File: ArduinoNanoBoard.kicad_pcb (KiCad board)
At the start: 2 copper layers, 121.9 x 81.3 mm, 12 parts, among them J1 Conn_01x15_Male, J2 Conn_01x04_Male, J3 Conn_01x10_Male, J4 Conn_01x08_Male, J5 Conn_01x04_Male

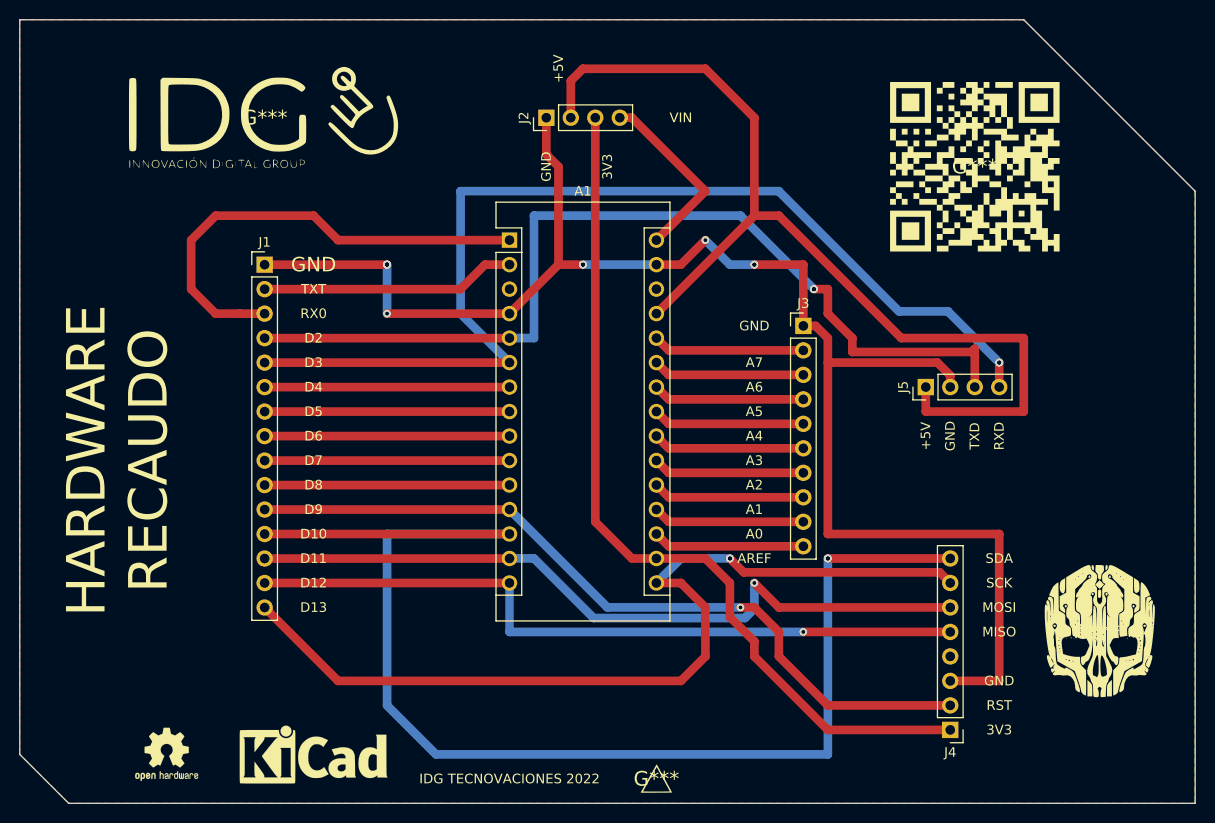
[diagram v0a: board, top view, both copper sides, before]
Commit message: BOPIR05 - ADD HOLES TO PCB
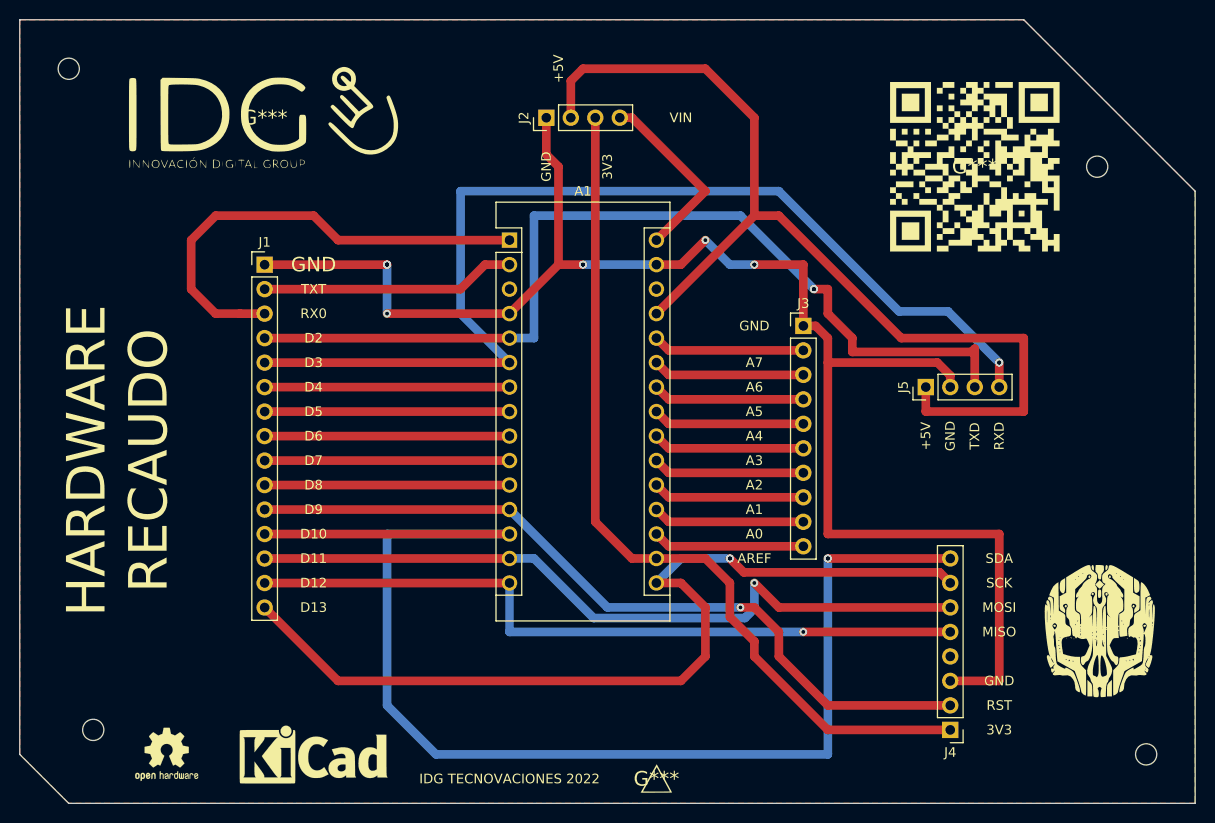
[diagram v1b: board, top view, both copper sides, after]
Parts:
- added REF**: MountingHole_2.2mm_M2, MountingHole:MountingHole_2.2mm_M2, F.Cu at (198.1, 132.1)
- added REF**: MountingHole_2.2mm_M2, MountingHole:MountingHole_2.2mm_M2, F.Cu at (88.9, 129.5)
- added REF**: MountingHole_2.2mm_M2, MountingHole:MountingHole_2.2mm_M2, F.Cu at (86.4, 61.0)
- added REF**: MountingHole_2.2mm_M2, MountingHole:MountingHole_2.2mm_M2, F.Cu at (193.0, 71.1)
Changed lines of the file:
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@@
       (svguseinch false)
       (svgprecision 6)
-      (excludeedgelayer true)
+      (excludeedgelayer false)
       (plotframeref false)
       (viasonmask false)
@@
       (drillshape 0)
       (scaleselection 1)
-      (outputdirectory "")
+      (outputdirectory "../gerberIdg/")
     )
   )
@@
       ) (layer "F.SilkS") (width 0.01) (fill solid))
   )
+  (footprint "MountingHole:MountingHole_2.2mm_M2" (layer "F.Cu")
+    (at 198.12 132.08)
+    (descr "Mounting Hole 2.2mm, no annular, M2")
+    (tags "mounting hole 2.2mm no annular m2")
+    (attr exclude_from_pos_files exclude_from_bom)
+    (fp_text reference "REF**" (at 0 -3.2) (layer "F.SilkS") hide
+      (effects (font (size 1 1) (thickness 0.15)))
+    )
+    (fp_text value "MountingHole_2.2mm_M2" (at 0 3.2) (layer "F.Fab")
+      (effects (font (size 1 1) (thickness 0.15)))
+    )
+    (fp_text user "${REFERENCE}" (at 0.3 0) (layer "F.Fab") hide
+      (effects (font (size 1 1) (thickness 0.15)))
+    )
+    (fp_circle (center 0 0) (end 2.2 0) (layer "Cmts.User") (width 0.15) (fill none))
+    (fp_circle (center 0 0) (end 2.45 0) (layer "F.CrtYd") (width 0.05) (fill none))
+    (pad "" np_thru_hole circle locked (at 0 0) (size 2.2 2.2) (drill 2.2) (layers *.Cu *.Mask))
+  )
   (footprint "Connector_PinHeader_2.54mm:PinHeader_1x08_P2.54mm_Vertical" (layer "F.Cu")
     (at 177.8 129.54 180)
@@
       ) (layer "F.SilkS") (width 0) (fill solid))
   )
+  (footprint "MountingHole:MountingHole_2.2mm_M2" (layer "F.Cu")
+    (at 88.9 129.54)
+    (descr "Mounting Hole 2.2mm, no annular, M2")
+    (tags "mounting hole 2.2mm no annular m2")
+    (attr exclude_from_pos_files exclude_from_bom)
+    (fp_text reference "REF**" (at 0 -3.2) (layer "F.SilkS") hide
+      (effects (font (size 1 1) (thickness 0.15)))
+    )
+    (fp_text value "MountingHole_2.2mm_M2" (at 0 3.2) (layer "F.Fab")
+      (effects (font (size 1 1) (thickness 0.15)))
+    )
+    (fp_text user "${REFERENCE}" (at 0.3 0) (layer "F.Fab") hide
+      (effects (font (size 1 1) (thickness 0.15)))
+    )
+    (fp_circle (center 0 0) (end 2.2 0) (layer "Cmts.User") (width 0.15) (fill none))
+    (fp_circle (center 0 0) (end 2.45 0) (layer "F.CrtYd") (width 0.05) (fill none))
+    (pad "" np_thru_hole circle locked (at 0 0) (size 2.2 2.2) (drill 2.2) (layers *.Cu *.Mask))
+  )
   (footprint "Module:Arduino_Nano" (layer "F.Cu")
     (at 132.08 78.74)
@@
     )
   )
+  (footprint "MountingHole:MountingHole_2.2mm_M2" (layer "F.Cu")
+    (at 86.36 60.96)
+    (descr "Mounting Hole 2.2mm, no annular, M2")
+    (tags "mounting hole 2.2mm no annular m2")
+    (attr exclude_from_pos_files exclude_from_bom)
+    (fp_text reference "REF**" (at 0 -3.2) (layer "F.SilkS") hide
+      (effects (font (size 1 1) (thickness 0.15)))
+    )
+    (fp_text value "MountingHole_2.2mm_M2" (at 0 3.2) (layer "F.Fab")
+      (effects (font (size 1 1) (thickness 0.15)))
+    )
+    (fp_text user "${REFERENCE}" (at 0.3 0) (layer "F.Fab") hide
+      (effects (font (size 1 1) (thickness 0.15)))
+    )
+    (fp_circle (center 0 0) (end 2.2 0) (layer "Cmts.User") (width 0.15) (fill none))
+    (fp_circle (center 0 0) (end 2.45 0) (layer "F.CrtYd") (width 0.05) (fill none))
+    (pad "" np_thru_hole circle locked (at 0 0) (size 2.2 2.2) (drill 2.2) (layers F&B.Cu *.Mask))
+  )
   (footprint "Connector_PinHeader_2.54mm:PinHeader_1x10_P2.54mm_Vertical" (layer "F.Cu")
     (at 162.56 87.635)
@@
     )
   )
+  (footprint "MountingHole:MountingHole_2.2mm_M2" (layer "F.Cu")
+    (at 193.04 71.12)
+    (descr "Mounting Hole 2.2mm, no annular, M2")
+    (tags "mounting hole 2.2mm no annular m2")
+    (attr exclude_from_pos_files exclude_from_bom)
+    (fp_text reference "REF**" (at 0 -3.2) (layer "F.SilkS") hide
+      (effects (font (size 1 1) (thickness 0.15)))
+    )
+    (fp_text value "MountingHole_2.2mm_M2" (at 0 3.2) (layer "F.Fab")
+      (effects (font (size 1 1) (thickness 0.15)))
+    )
+    (fp_text user "${REFERENCE}" (at 0.3 0) (layer "F.Fab") hide
+      (effects (font (size 1 1) (thickness 0.15)))
+    )
+    (fp_circle (center 0 0) (end 2.2 0) (layer "Cmts.User") (width 0.15) (fill none))
+    (fp_circle (center 0 0) (end 2.45 0) (layer "F.CrtYd") (width 0.05) (fill none))
+    (pad "" np_thru_hole circle locked (at 0 0) (size 2.2 2.2) (drill 2.2) (layers *.Cu *.Mask))
+  )
   (footprint "idg:idg" (layer "F.Cu")
     (at 106.68 66.04)
@@
   )
   (dimension (type aligned) (layer "F.SilkS")
-    (pts (xy 185.42 55.88) (xy 203.2 73.66))
+    (pts (xy 182.88 55.88) (xy 200.66 73.66))
     (height 0)
-    (gr_text "25,1447 mm" (at 195.123173 63.956827 315) (layer "F.SilkS")
+    (gr_text "25,1447 mm" (at 192.583173 63.956827 315) (layer "F.SilkS")
       (effects (font (size 1 1) (thickness 0.15)))
     )
